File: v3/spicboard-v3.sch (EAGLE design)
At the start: 40 parts, among them IC1 74HC595, Q1 BC557, Q2 BC557

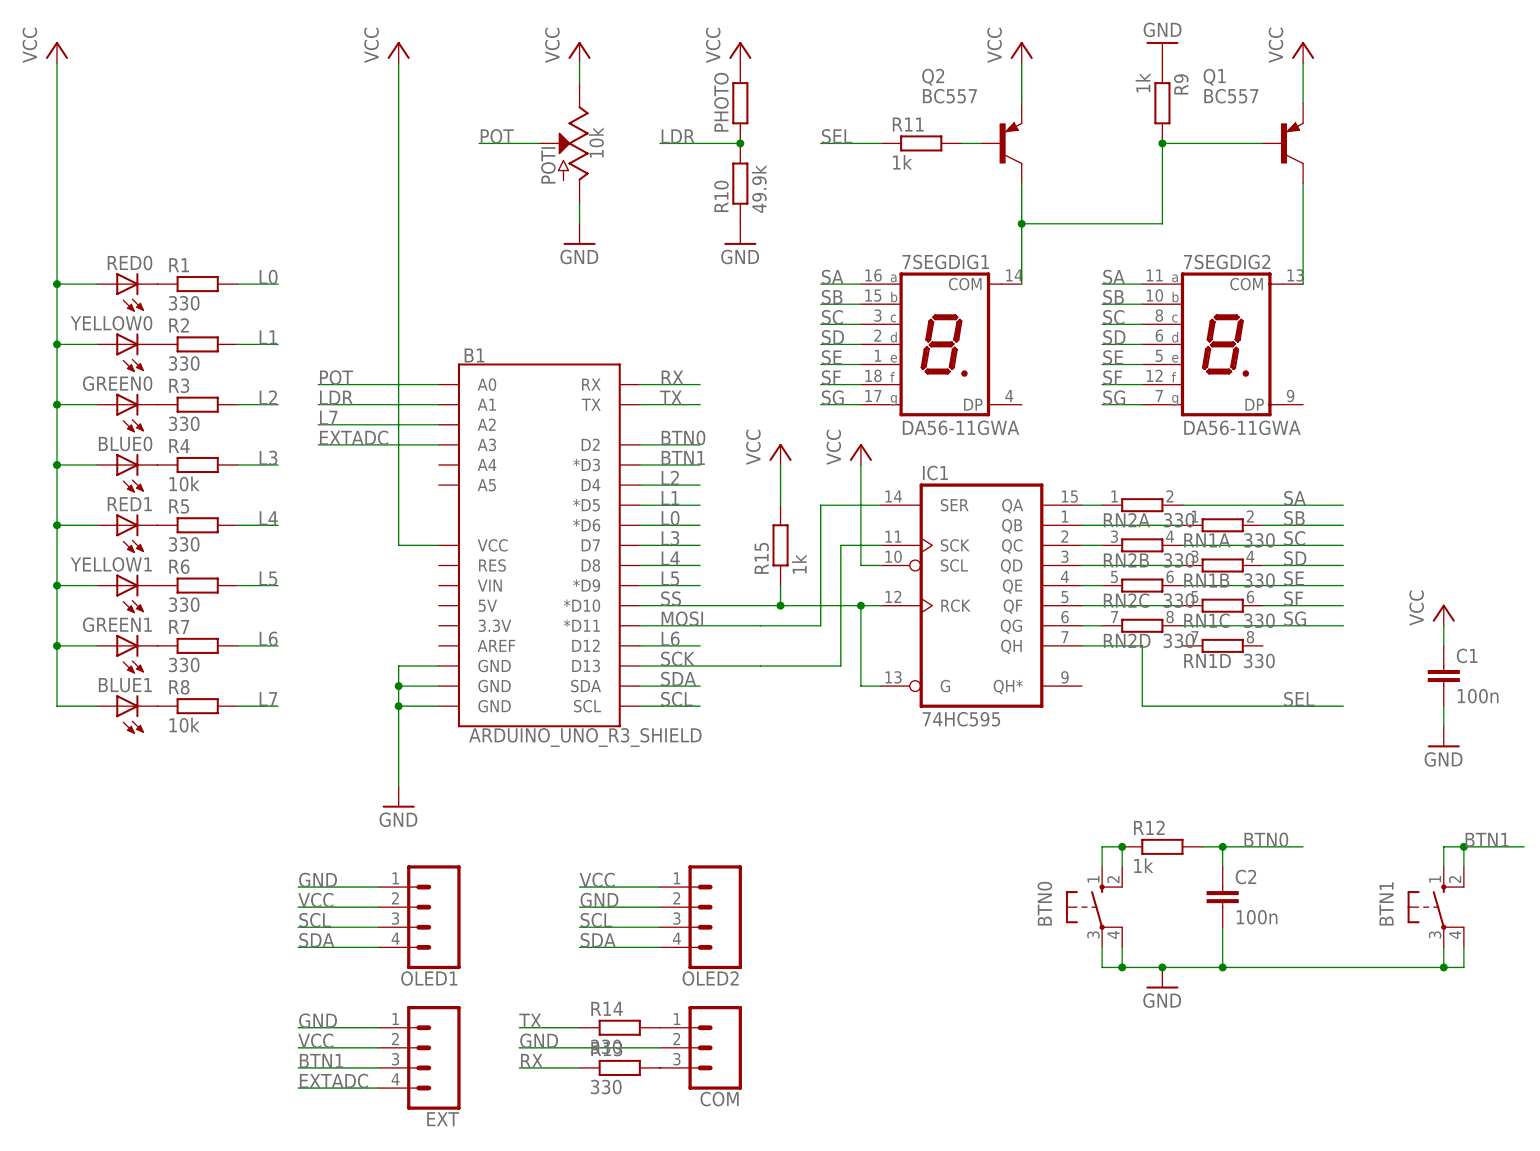
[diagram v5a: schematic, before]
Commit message: LED Pin geaendert
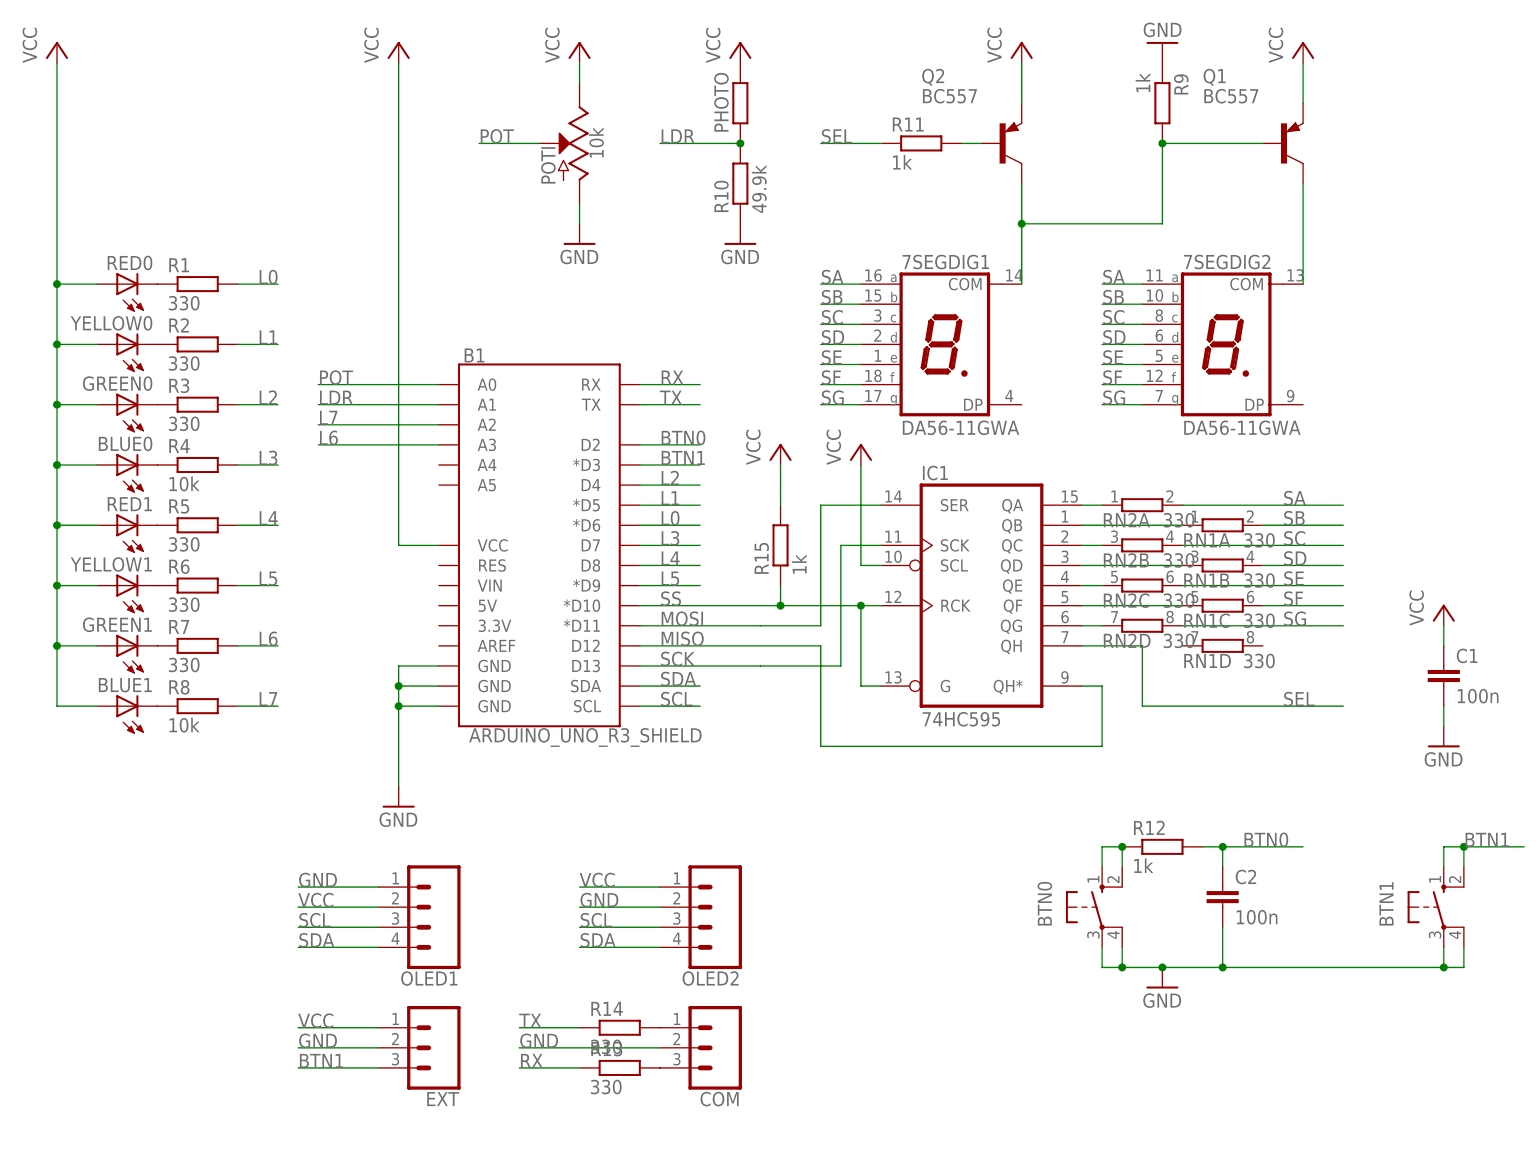
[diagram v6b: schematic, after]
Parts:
- EXT: device SparkFun-Connectors:CONN_04 -> SparkFun-Connectors:CONN_03
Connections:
- removed net EXTADC: B1.A3, EXT.4
- new net MISO: B1.D12, IC1A.QH*
- net GND: now also EXT.2; no longer EXT.1
- net L6: now also B1.A3; no longer B1.D12
- net VCC: now also EXT.1; no longer EXT.2
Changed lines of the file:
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@@
 <part name="OLED1" library="SparkFun-Connectors" deviceset="CONN_04" device=""/>
 <part name="OLED2" library="SparkFun-Connectors" deviceset="CONN_04" device=""/>
-<part name="EXT" library="SparkFun-Connectors" deviceset="CONN_04" device=""/>
 <part name="COM" library="SparkFun-Connectors" deviceset="CONN_03" device=""/>
 <part name="R15" library="resistor" deviceset="R-EU_" device="0207/10" value="1k"/>
 <part name="P+9" library="supply1" deviceset="VCC" device=""/>
+<part name="EXT" library="SparkFun-Connectors" deviceset="CONN_03" device=""/>
 </parts>
 <sheets>
@@
 <instance part="OLED1" gate="G$1" x="43.18" y="0" rot="R180"/>
 <instance part="OLED2" gate="G$1" x="78.74" y="0" rot="R180"/>
-<instance part="EXT" gate="G$1" x="43.18" y="-17.78" rot="R180"/>
 <instance part="COM" gate="J$1" x="81.28" y="-17.78" rot="R180"/>
 <instance part="R15" gate="G$1" x="88.9" y="45.72" rot="R90"/>
 <instance part="P+9" gate="VCC" x="88.9" y="58.42"/>
+<instance part="EXT" gate="J$1" x="45.72" y="-17.78" rot="R180"/>
 </instances>
 <busses>
@@
 </segment>
 <segment>
-<wire x1="38.1" y1="-17.78" x2="27.94" y2="-17.78" width="0.1524" layer="91"/>
-<label x="27.94" y="-17.78" size="1.778" layer="95"/>
-<pinref part="EXT" gate="G$1" pin="2"/>
+<wire x1="38.1" y1="-15.24" x2="27.94" y2="-15.24" width="0.1524" layer="91"/>
+<label x="27.94" y="-15.24" size="1.778" layer="95"/>
+<pinref part="EXT" gate="J$1" pin="1"/>
 </segment>
 <segment>
@@
 </segment>
 <segment>
-<wire x1="38.1" y1="-15.24" x2="27.94" y2="-15.24" width="0.1524" layer="91"/>
-<label x="27.94" y="-15.24" size="1.778" layer="95"/>
-<pinref part="EXT" gate="G$1" pin="1"/>
+<wire x1="38.1" y1="-17.78" x2="27.94" y2="-17.78" width="0.1524" layer="91"/>
+<label x="27.94" y="-17.78" size="1.778" layer="95"/>
+<pinref part="EXT" gate="J$1" pin="2"/>
 </segment>
 </net>
@@
 </segment>
 <segment>
-<pinref part="B1" gate="G$1" pin="D12"/>
-<wire x1="71.12" y1="33.02" x2="78.74" y2="33.02" width="0.1524" layer="91"/>
-<label x="73.66" y="33.02" size="1.778" layer="95"/>
+<pinref part="B1" gate="G$1" pin="A3"/>
+<wire x1="45.72" y1="58.42" x2="30.48" y2="58.42" width="0.1524" layer="91"/>
+<label x="30.48" y="58.42" size="1.778" layer="95"/>
 </segment>
 </net>
@@
 <wire x1="38.1" y1="-20.32" x2="27.94" y2="-20.32" width="0.1524" layer="91"/>
 <label x="27.94" y="-20.32" size="1.778" layer="95"/>
-<pinref part="EXT" gate="G$1" pin="3"/>
-</segment>
-</net>
-<net name="EXTADC" class="0">
-<segment>
-<wire x1="38.1" y1="-22.86" x2="27.94" y2="-22.86" width="0.1524" layer="91"/>
-<label x="27.94" y="-22.86" size="1.778" layer="95"/>
-<pinref part="EXT" gate="G$1" pin="4"/>
-</segment>
-<segment>
-<pinref part="B1" gate="G$1" pin="A3"/>
-<wire x1="45.72" y1="58.42" x2="30.48" y2="58.42" width="0.1524" layer="91"/>
-<label x="30.48" y="58.42" size="1.778" layer="95"/>
+<pinref part="EXT" gate="J$1" pin="3"/>
 </segment>
 </net>
@@
 </segment>
 </net>
+<net name="MISO" class="0">
+<segment>
+<pinref part="B1" gate="G$1" pin="D12"/>
+<wire x1="71.12" y1="33.02" x2="93.98" y2="33.02" width="0.1524" layer="91"/>
+<wire x1="93.98" y1="33.02" x2="93.98" y2="20.32" width="0.1524" layer="91"/>
+<wire x1="93.98" y1="20.32" x2="129.54" y2="20.32" width="0.1524" layer="91"/>
+<wire x1="129.54" y1="20.32" x2="129.54" y2="27.94" width="0.1524" layer="91"/>
+<pinref part="IC1" gate="A" pin="QH*"/>
+<wire x1="129.54" y1="27.94" x2="127" y2="27.94" width="0.1524" layer="91"/>
+<label x="73.66" y="33.02" size="1.778" layer="95"/>
+</segment>
+</net>

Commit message: SPiCboard: Bauteile ersetzt (PAD-Größe)
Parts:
- 7SEG: device display-kingbright:DA56-11GWA -> spicboard-v3:DA56-11GWA
- BLUE0, BLUE1, GREEN0, GREEN1, RED0, RED1, YELLOW0, YELLOW1: device led:LED5MM -> spicboard-v3:LED5MM
- C1, C2: device capacitor-wima:C2.5/2 -> spicboard-v3:C2.5/2
- R1, R10, R11, R12, R13, R14, R15, R2, R3, R4, R5, R6, R7, R8, R9: device resistor:R-EU_0207/10 -> spicboard-v3:R-EU_0207/10
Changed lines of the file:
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@@
 <parts>
 <part name="B1" library="spicboard-v3" deviceset="ARDUINO_UNO_R3_SHIELD" device="" value="ARDUINO_UNO_R3_SHIELD"/>
-<part name="RED0" library="led" deviceset="LED" device="5MM"/>
-<part name="YELLOW0" library="led" deviceset="LED" device="5MM"/>
-<part name="GREEN0" library="led" deviceset="LED" device="5MM"/>
-<part name="BLUE0" library="led" deviceset="LED" device="5MM"/>
-<part name="RED1" library="led" deviceset="LED" device="5MM"/>
-<part name="YELLOW1" library="led" deviceset="LED" device="5MM"/>
-<part name="GREEN1" library="led" deviceset="LED" device="5MM"/>
-<part name="BLUE1" library="led" deviceset="LED" device="5MM"/>
-<part name="R1" library="resistor" deviceset="R-EU_" device="0207/10" value="330"/>
-<part name="R2" library="resistor" deviceset="R-EU_" device="0207/10" value="330"/>
-<part name="R3" library="resistor" deviceset="R-EU_" device="0207/10" value="330"/>
-<part name="R4" library="resistor" deviceset="R-EU_" device="0207/10" value="10k"/>
-<part name="R5" library="resistor" deviceset="R-EU_" device="0207/10" value="330"/>
-<part name="R6" library="resistor" deviceset="R-EU_" device="0207/10" value="330"/>
-<part name="R7" library="resistor" deviceset="R-EU_" device="0207/10" value="330"/>
-<part name="R8" library="resistor" deviceset="R-EU_" device="0207/10" value="10k"/>
+<part name="RED0" library="spicboard-v3" deviceset="LED" device="5MM"/>
+<part name="YELLOW0" library="spicboard-v3" deviceset="LED" device="5MM"/>
+<part name="GREEN0" library="spicboard-v3" deviceset="LED" device="5MM"/>
+<part name="BLUE0" library="spicboard-v3" deviceset="LED" device="5MM"/>
+<part name="RED1" library="spicboard-v3" deviceset="LED" device="5MM"/>
+<part name="YELLOW1" library="spicboard-v3" deviceset="LED" device="5MM"/>
+<part name="GREEN1" library="spicboard-v3" deviceset="LED" device="5MM"/>
+<part name="BLUE1" library="spicboard-v3" deviceset="LED" device="5MM"/>
+<part name="R1" library="spicboard-v3" deviceset="R-EU_" device="0207/10" value="330"/>
+<part name="R2" library="spicboard-v3" deviceset="R-EU_" device="0207/10" value="330"/>
+<part name="R3" library="spicboard-v3" deviceset="R-EU_" device="0207/10" value="330"/>
+<part name="R4" library="spicboard-v3" deviceset="R-EU_" device="0207/10" value="10k"/>
+<part name="R5" library="spicboard-v3" deviceset="R-EU_" device="0207/10" value="330"/>
+<part name="R6" library="spicboard-v3" deviceset="R-EU_" device="0207/10" value="330"/>
+<part name="R7" library="spicboard-v3" deviceset="R-EU_" device="0207/10" value="330"/>
+<part name="R8" library="spicboard-v3" deviceset="R-EU_" device="0207/10" value="10k"/>
 <part name="IC1" library="74xx-eu" deviceset="74*595" device="N" technology="HC" value="74HC595"/>
 <part name="PHOTO" library="spicboard-v3" deviceset="LDR" device="" value="LDR"/>
@@
 <part name="Q1" library="transistor-pnp" deviceset="BC557*" device=""/>
 <part name="Q2" library="transistor-pnp" deviceset="BC557*" device=""/>
-<part name="7SEG" library="display-kingbright" deviceset="DA56-11" device="" technology="GWA" value="DA56-11GWA"/>
+<part name="7SEG" library="spicboard-v3" deviceset="DA56-11" device="" technology="GWA" value="DA56-11GWA"/>
 <part name="GND1" library="supply1" deviceset="GND" device=""/>
 <part name="P+1" library="supply1" deviceset="VCC" device=""/>
@@
 <part name="GND2" library="supply1" deviceset="GND" device=""/>
 <part name="P+4" library="supply1" deviceset="VCC" device=""/>
-<part name="R10" library="resistor" deviceset="R-EU_" device="0207/10" value="49.9k"/>
+<part name="R10" library="spicboard-v3" deviceset="R-EU_" device="0207/10" value="49.9k"/>
 <part name="P+5" library="supply1" deviceset="VCC" device=""/>
 <part name="GND3" library="supply1" deviceset="GND" device=""/>
 <part name="P+6" library="supply1" deviceset="VCC" device=""/>
 <part name="GND4" library="supply1" deviceset="GND" device=""/>
-<part name="R9" library="resistor" deviceset="R-EU_" device="0207/10" value="1k"/>
-<part name="R11" library="resistor" deviceset="R-EU_" device="0207/10" value="1k"/>
+<part name="R9" library="spicboard-v3" deviceset="R-EU_" device="0207/10" value="1k"/>
+<part name="R11" library="spicboard-v3" deviceset="R-EU_" device="0207/10" value="1k"/>
 <part name="P+7" library="supply1" deviceset="VCC" device=""/>
-<part name="C1" library="capacitor-wima" deviceset="C" device="2.5/2" value="100n"/>
+<part name="C1" library="spicboard-v3" deviceset="C" device="2.5/2" value="100n"/>
 <part name="P+8" library="supply1" deviceset="VCC" device=""/>
 <part name="GND6" library="supply1" deviceset="GND" device=""/>
-<part name="R12" library="resistor" deviceset="R-EU_" device="0207/10" value="1k"/>
-<part name="C2" library="capacitor-wima" deviceset="C" device="2.5/2" value="100n"/>
+<part name="R12" library="spicboard-v3" deviceset="R-EU_" device="0207/10" value="1k"/>
+<part name="C2" library="spicboard-v3" deviceset="C" device="2.5/2" value="100n"/>
 <part name="GND7" library="supply1" deviceset="GND" device=""/>
-<part name="R13" library="resistor" deviceset="R-EU_" device="0207/10" value="330"/>
-<part name="R14" library="resistor" deviceset="R-EU_" device="0207/10" value="330"/>
+<part name="R13" library="spicboard-v3" deviceset="R-EU_" device="0207/10" value="330"/>
+<part name="R14" library="spicboard-v3" deviceset="R-EU_" device="0207/10" value="330"/>
 <part name="BTN0" library="switch-omron" deviceset="10-XX" device=""/>
 <part name="BTN1" library="switch-omron" deviceset="10-XX" device=""/>
@@
 <part name="OLED2" library="SparkFun-Connectors" deviceset="CONN_04" device=""/>
 <part name="COM" library="SparkFun-Connectors" deviceset="CONN_03" device=""/>
-<part name="R15" library="resistor" deviceset="R-EU_" device="0207/10" value="1k"/>
+<part name="R15" library="spicboard-v3" deviceset="R-EU_" device="0207/10" value="1k"/>
 <part name="P+9" library="supply1" deviceset="VCC" device=""/>
 <part name="EXT" library="SparkFun-Connectors" deviceset="CONN_03" device=""/>

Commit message: SPiCboard: Bauteile aus Standard-Bibliotheken
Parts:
- BLUE0, BLUE1, GREEN0, GREEN1, RED0, RED1, YELLOW0, YELLOW1: device spicboard-v3:LED5MM -> led:LED5MM
- R1, R10, R11, R12, R13, R14, R15, R2, R3, R4, R5, R6, R7, R8, R9: device spicboard-v3:R-EU_0207/10 -> resistor:R-EU_0207/10
